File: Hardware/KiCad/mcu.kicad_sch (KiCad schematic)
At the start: 10 parts, among them U3 STM32F427ZGTx, Y1 8 MHz, Y2 32 kHz

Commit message: R7 update
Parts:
- R7: value (none) -> 0R; footprint (none) -> Resistor_SMD:R_0402_1005Metric; symbol Device:R -> Device:R_Small

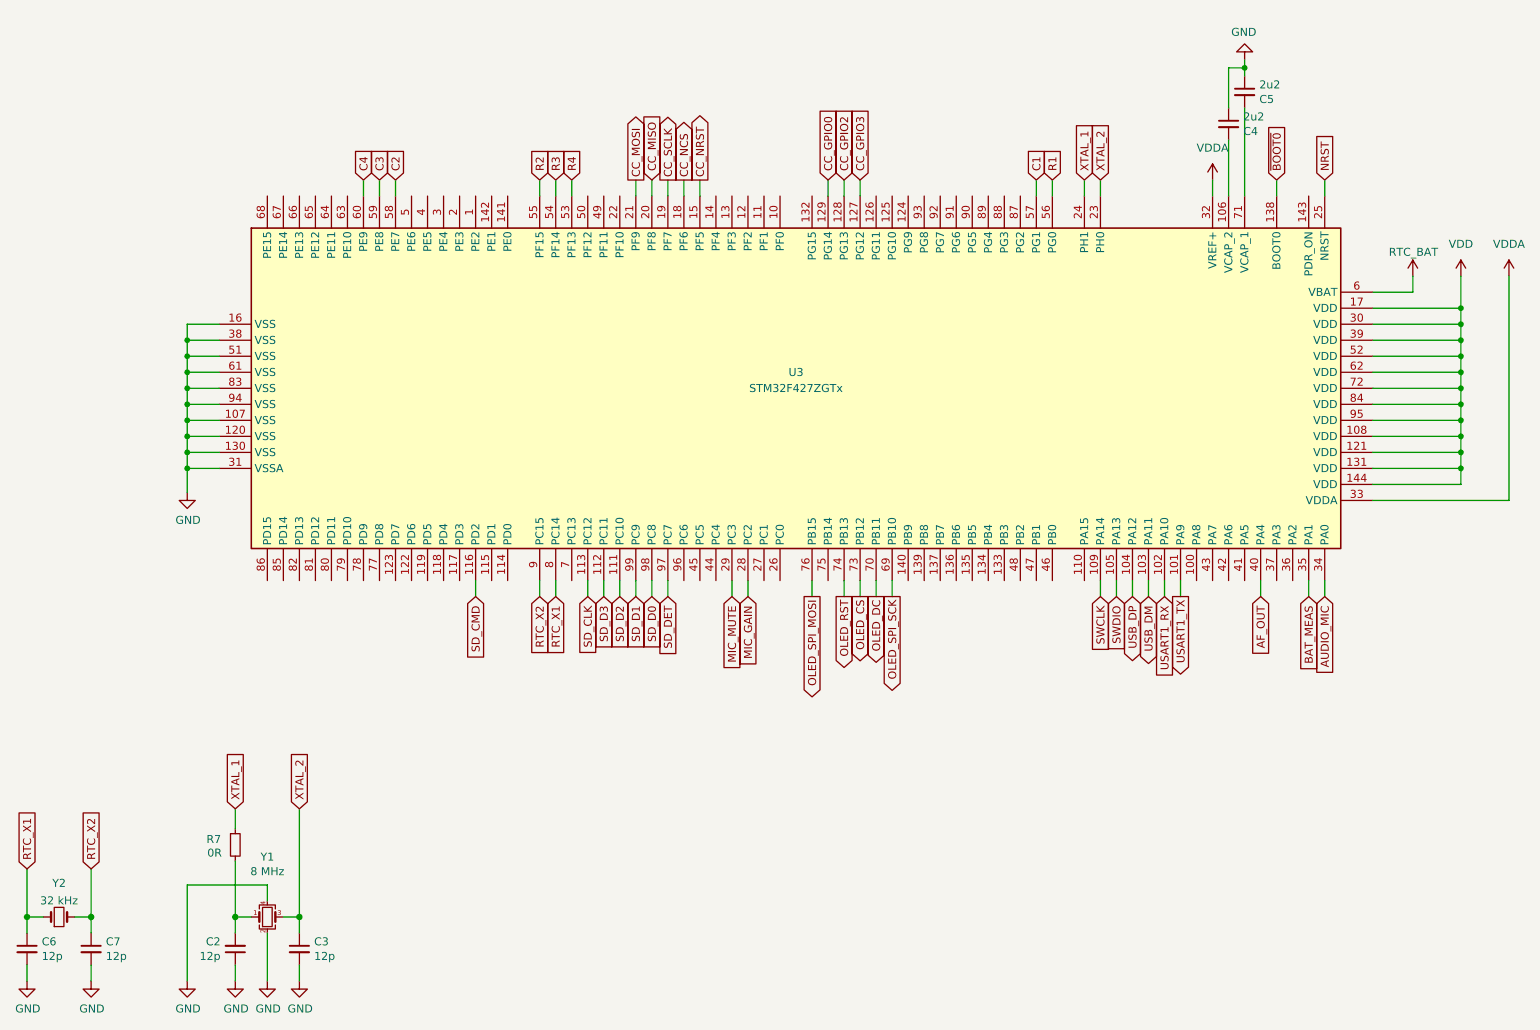
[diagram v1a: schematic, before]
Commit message: fixup PTT/Audio (Issue 14), add RGB LED (Issue 26), Connect LEDs to MCU & add them to the .ioc file
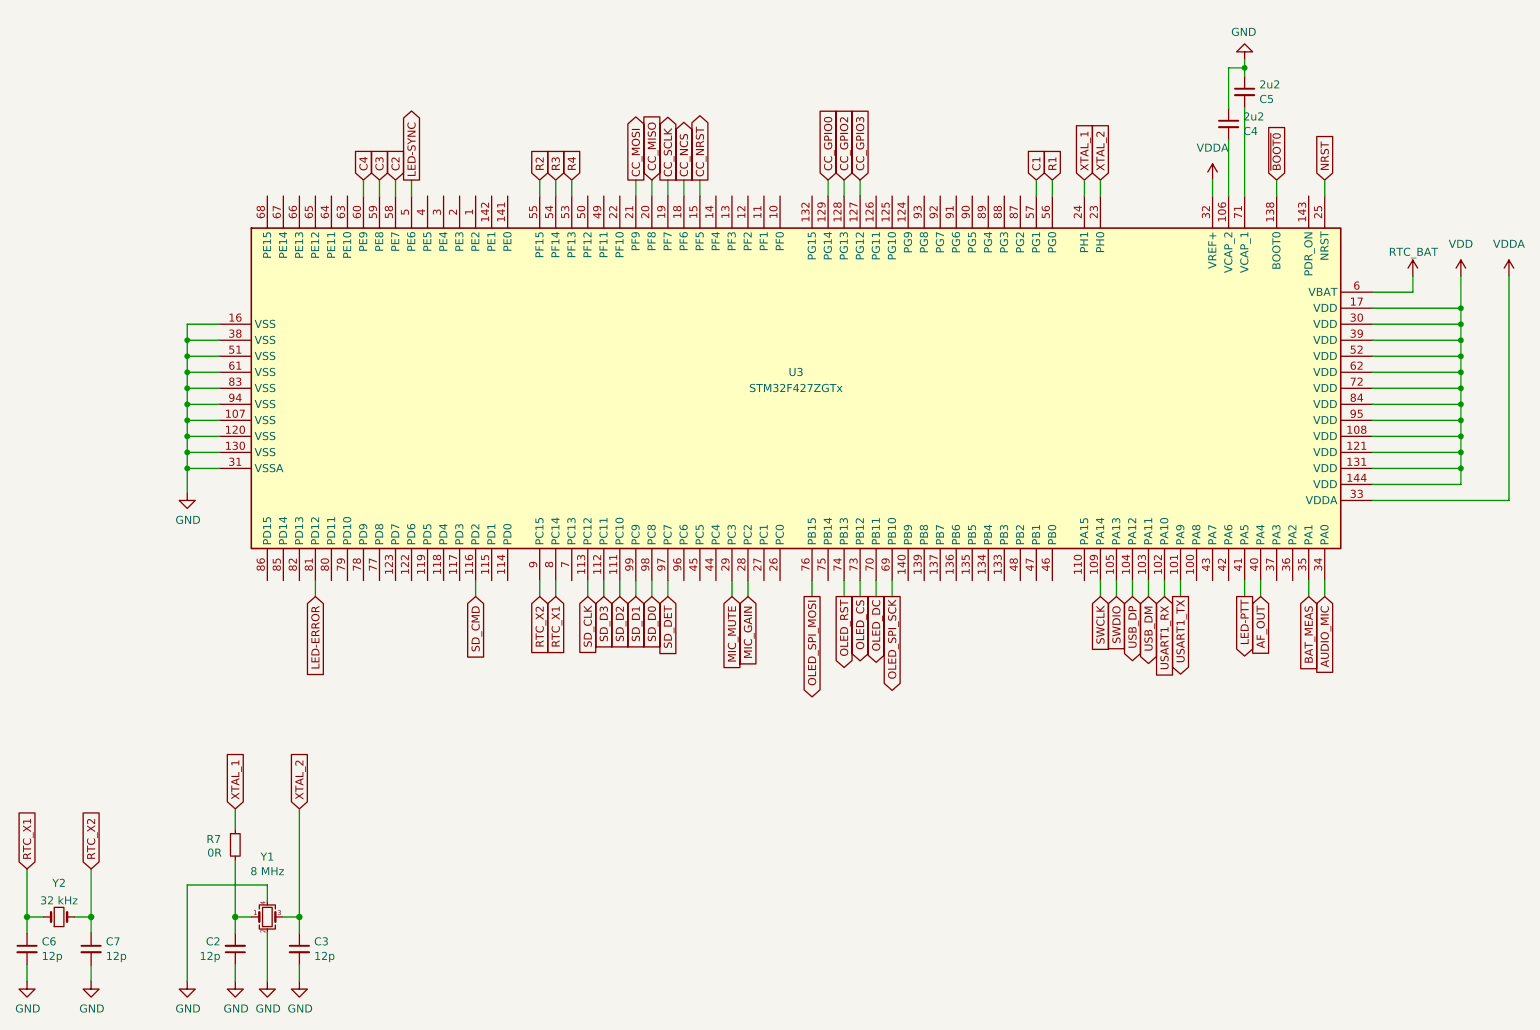
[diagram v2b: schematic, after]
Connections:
- net LED-PTT: now reaches U3.41 (PA5)
- net LED-SYNC: now reaches U3.5 (PE6)
- net LED-ERROR: now reaches U3.81 (PD12)
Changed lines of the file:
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@@
     (stroke (width 0) (type solid) (color 0 0 0 0))
+  )
+  (wire (pts (xy 88.9 50.8) (xy 88.9 53.34))
+    (stroke (width 0) (type default) (color 0 0 0 0))
   )
   (wire (pts (xy 53.34 162.56) (xy 53.34 177.8))
@@
     (stroke (width 0) (type default) (color 0 0 0 0))
   )
+  (wire (pts (xy 73.66 114.3) (xy 73.66 116.84))
+    (stroke (width 0) (type default) (color 0 0 0 0))
+  )
   (wire (pts (xy 53.34 76.2) (xy 53.34 73.66))
     (stroke (width 0) (type default) (color 0 0 0 0))
@@
     (stroke (width 0) (type default) (color 0 0 0 0))
   )
+  (wire (pts (xy 220.98 114.3) (xy 220.98 116.84))
+    (stroke (width 0) (type default) (color 0 0 0 0))
+  )
   (wire (pts (xy 220.98 31.75) (xy 220.98 33.02))
     (stroke (width 0) (type default) (color 0 0 0 0))
@@
     )
   )
+  (global_label "LED-SYNC" (shape output) (at 88.9 50.8 90) (fields_autoplaced)
+    (effects (font (size 1.27 1.27)) (justify left))
+    (property "Intersheet References" "${INTERSHEET_REFS}" (id 0) (at 88.8206 38.4688 90)
+      (effects (font (size 1.27 1.27)) (justify left) hide)
+    )
+  )
   (global_label "OLED_RST" (shape output) (at 157.48 116.84 270) (fields_autoplaced)
     (effects (font (size 1.27 1.27)) (justify right))
@@
     (property "Intersheet References" "${INTERSHEET_REFS}" (id 0) (at 38.0206 150.7126 90)
       (effects (font (size 1.27 1.27)) (justify left) hide)
+    )
+  )
+  (global_label "LED-ERROR" (shape input) (at 73.66 116.84 270) (fields_autoplaced)
+    (effects (font (size 1.27 1.27)) (justify right))
+    (property "Intersheet References" "${INTERSHEET_REFS}" (id 0) (at -81.28 378.46 0)
+      (effects (font (size 1.27 1.27)) hide)
     )
   )
@@
     )
   )
+  (global_label "LED-PTT" (shape output) (at 220.98 116.84 270) (fields_autoplaced)
+    (effects (font (size 1.27 1.27)) (justify right))
+    (property "Intersheet References" "${INTERSHEET_REFS}" (id 0) (at 220.9006 127.4779 90)
+      (effects (font (size 1.27 1.27)) (justify right) hide)
+    )
+  )

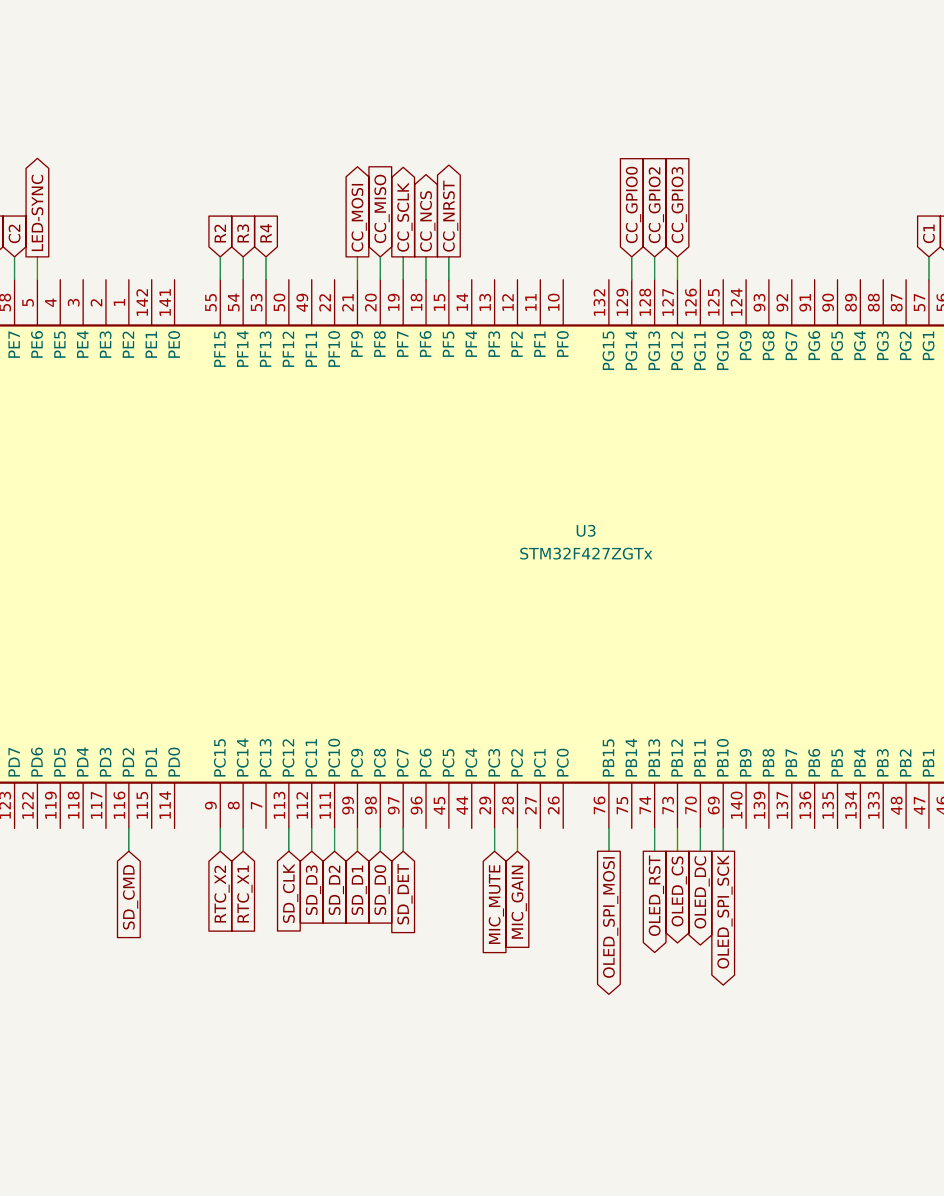
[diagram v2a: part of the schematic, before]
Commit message: add encoder & volume control, move SD_DET to accommodate encoder
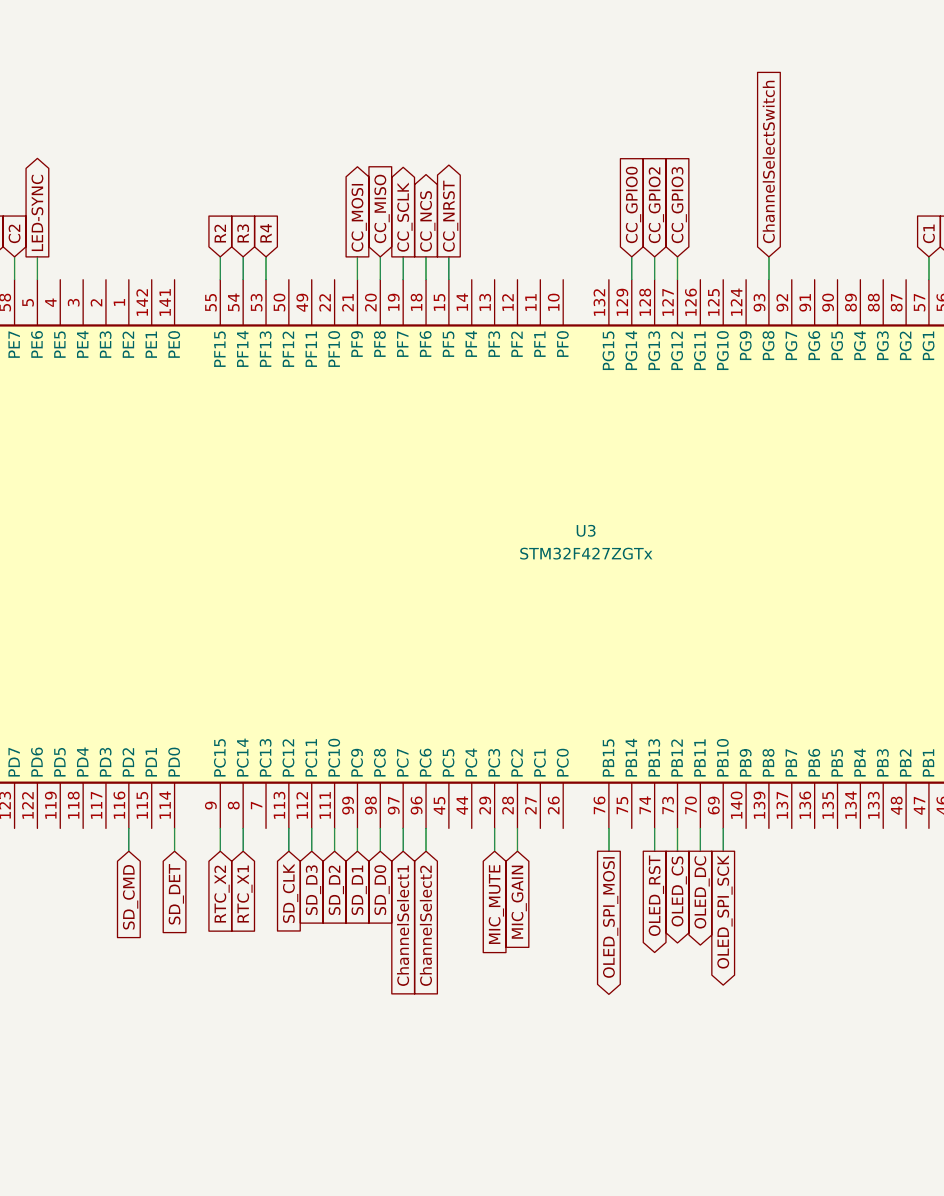
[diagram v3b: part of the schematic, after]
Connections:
- net SD_DET: now also U3.114 (PD0); no longer U3.97 (PC7)
- net ChannelSelectSwitch: now reaches U3.93 (PG8)
- net ChannelSelect2: now reaches U3.96 (PC6)
- new net ChannelSelect1: U3.97 (PC7)
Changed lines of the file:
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@@
+    (stroke (width 0) (type default) (color 0 0 0 0))
+  )
+  (wire (pts (xy 170.18 50.8) (xy 170.18 53.34))
     (stroke (width 0) (type default) (color 0 0 0 0))
   )
@@
     (stroke (width 0) (type default) (color 0 0 0 0))
   )
+  (wire (pts (xy 129.54 114.3) (xy 129.54 116.84))
+    (stroke (width 0) (type default) (color 0 0 0 0))
+  )
   (wire (pts (xy 233.68 50.8) (xy 233.68 53.34))
     (stroke (width 0) (type solid) (color 0 0 0 0))
@@
     (stroke (width 0) (type default) (color 0 0 0 0))
   )
+  (wire (pts (xy 132.08 114.3) (xy 132.08 116.84))
+    (stroke (width 0) (type default) (color 0 0 0 0))
+  )
   (wire (pts (xy 53.34 76.2) (xy 53.34 73.66))
     (stroke (width 0) (type default) (color 0 0 0 0))
@@
     (stroke (width 0) (type default) (color 0 0 0 0))
   )
-  (wire (pts (xy 129.54 114.3) (xy 129.54 116.84))
+  (wire (pts (xy 104.14 114.3) (xy 104.14 116.84))
     (stroke (width 0) (type default) (color 0 0 0 0))
   )
@@
     )
   )
+  (global_label "ChannelSelect1" (shape input) (at 129.54 116.84 270) (fields_autoplaced)
+    (effects (font (size 1.27 1.27)) (justify right))
+    (property "Intersheet References" "${INTERSHEET_REFS}" (id 0) (at 129.4606 133.9488 90)
+      (effects (font (size 1.27 1.27)) (justify right) hide)
+    )
+  )
   (global_label "USART1_TX" (shape output) (at 210.82 116.84 270) (fields_autoplaced)
     (effects (font (size 1.27 1.27)) (justify right))
@@
     )
   )
+  (global_label "ChannelSelect2" (shape input) (at 132.08 116.84 270) (fields_autoplaced)
+    (effects (font (size 1.27 1.27)) (justify right))
+    (property "Intersheet References" "${INTERSHEET_REFS}" (id 0) (at 132.0006 133.9488 90)
+      (effects (font (size 1.27 1.27)) (justify right) hide)
+    )
+  )
   (global_label "CC_NCS" (shape output) (at 132.08 50.8 90) (fields_autoplaced)
     (effects (font (size 1.27 1.27)) (justify left))
     (property "Intersheet References" "${INTERSHEET_REFS}" (id 0) (at 132.0006 41.0693 90)
+      (effects (font (size 1.27 1.27)) (justify left) hide)
+    )
+  )
+  (global_label "ChannelSelectSwitch" (shape input) (at 170.18 50.8 90) (fields_autoplaced)
+    (effects (font (size 1.27 1.27)) (justify left))
+    (property "Intersheet References" "${INTERSHEET_REFS}" (id 0) (at 170.1006 28.7926 90)
       (effects (font (size 1.27 1.27)) (justify left) hide)
     )
@@
     )
   )
-  (global_label "SD_DET" (shape input) (at 129.54 116.84 270) (fields_autoplaced)
-    (effects (font (size 1.27 1.27)) (justify right))
-    (property "Intersheet References" "${INTERSHEET_REFS}" (id 0) (at 129.4606 126.0869 90)
-      (effects (font (size 1.27 1.27)) (justify right) hide)
-    )
+  (global_label "SD_DET" (shape input) (at 104.14 116.84 270) (fields_autoplaced)
+    (effects (font (size 1.27 1.27)) (justify right))
+    (property "Intersheet References" "${INTERSHEET_REFS}" (id 0) (at 104.0606 126.0869 90)
+      (effects (font (size 1.27 1.27)) (justify right) hide)
+    )

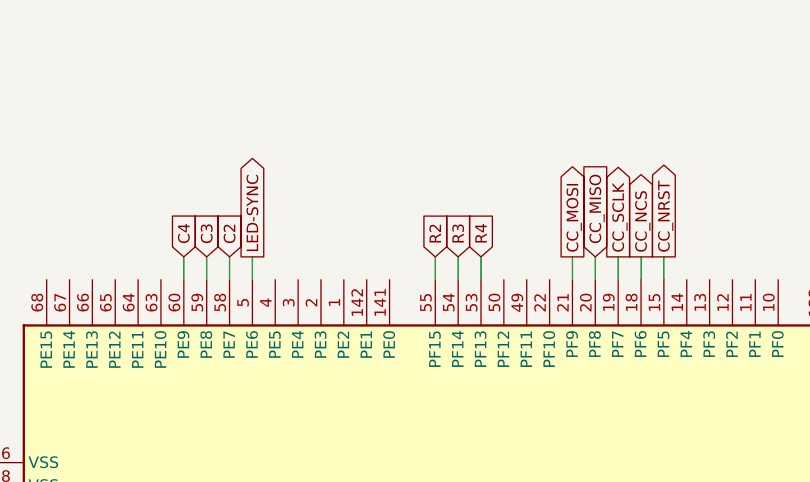
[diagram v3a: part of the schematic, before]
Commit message: Minor corrections
- fixed microphone connection and part values
- added a few TPs
- changed C27 footprint
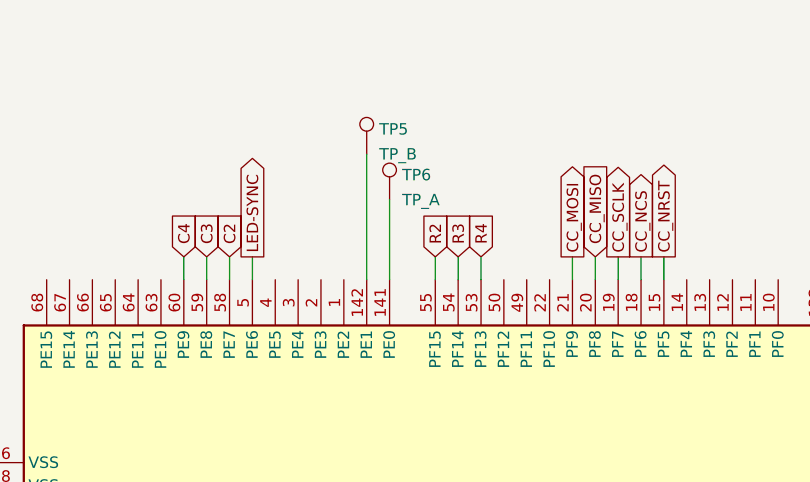
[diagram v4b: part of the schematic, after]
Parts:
- added TP5: TP_B, TestPoint:TestPoint_Pad_D1.0mm, symbol Connector:TestPoint
- added TP6: TP_A, TestPoint:TestPoint_Pad_D1.0mm, symbol Connector:TestPoint
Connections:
- net at U3.141 (PE0): now also TP6.1
- net at U3.142 (PE1): now also TP5.1
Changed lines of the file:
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@@
+    (stroke (width 0) (type default) (color 0 0 0 0))
+  )
+  (wire (pts (xy 104.14 44.45) (xy 104.14 53.34))
     (stroke (width 0) (type default) (color 0 0 0 0))
   )
@@
   )
   (wire (pts (xy 134.62 50.8) (xy 134.62 53.34))
+    (stroke (width 0) (type default) (color 0 0 0 0))
+  )
+  (wire (pts (xy 101.6 39.37) (xy 101.6 53.34))
     (stroke (width 0) (type default) (color 0 0 0 0))
   )
@@
     )
     (property "Datasheet" "" (id 3) (at 66.04 177.8 0)
+      (effects (font (size 1.27 1.27)) hide)
+    )
+    (pin "1")
+  )
+  (symbol (lib_id "Connector:TestPoint") (at 101.6 39.37 0) (unit 1)
+    (in_bom yes) (on_board yes) (fields_autoplaced)
+    (property "Reference" "TP5" (id 0) (at 102.9971 36.62 0)
+      (effects (font (size 1.27 1.27)) (justify left))
+    )
+    (property "Value" "TP_B" (id 1) (at 102.9971 39.3951 0)
+      (effects (font (size 1.27 1.27)) (justify left))
+    )
+    (property "Footprint" "TestPoint:TestPoint_Pad_D1.0mm" (id 2) (at 106.68 39.37 0)
+      (effects (font (size 1.27 1.27)) hide)
+    )
+    (property "Datasheet" "~" (id 3) (at 106.68 39.37 0)
       (effects (font (size 1.27 1.27)) hide)
     )
@@
     (pin "2")
   )
+  (symbol (lib_id "Connector:TestPoint") (at 104.14 44.45 0) (unit 1)
+    (in_bom yes) (on_board yes) (fields_autoplaced)
+    (property "Reference" "TP6" (id 0) (at 105.5371 41.7 0)
+      (effects (font (size 1.27 1.27)) (justify left))
+    )
+    (property "Value" "TP_A" (id 1) (at 105.5371 44.4751 0)
+      (effects (font (size 1.27 1.27)) (justify left))
+    )
+    (property "Footprint" "TestPoint:TestPoint_Pad_D1.0mm" (id 2) (at 109.22 44.45 0)
+      (effects (font (size 1.27 1.27)) hide)
+    )
+    (property "Datasheet" "~" (id 3) (at 109.22 44.45 0)
+      (effects (font (size 1.27 1.27)) hide)
+    )
+    (pin "1")
+  )
   (symbol (lib_id "power:GND") (at 220.98 31.75 180) (unit 1)
